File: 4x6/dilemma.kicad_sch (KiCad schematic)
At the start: 308 parts, among them J1 USB_C_Receptacle_USB2.0, J102 NA_serial, J105 NA_Conn_01x04_Female, J113 Cirque, J3 NA_GC9A01, J4 Conn_01x05, J5 NA_Conn_01x02, J5001 USB_C_Receptacle_USB2.0, J5002 NA_Conn_01x02, J5003 NA_serial, J5004 NA_GC9A01, J5005 NA_Conn_01x04_Female, J5007 Cirque, J5008 Conn_01x05, J5009 Conn_01x05, J5010 Conn_01x05, SW1 SW_Push, SW101 NA_SW_Push, SW102 NA_SW_Push, SW103 NA_SW_Push, SW104 NA_SW_Push, SW105 NA_SW_Push, SW106 NA_SW_Push, SW107 NA_SW_Push, SW108 NA_SW_Push, SW109 NA_SW_Push, SW112 NA_SW_Push, SW113 NA_SW_Push, SW114 NA_SW_Push, SW115 NA_SW_Push, SW116 NA_SW_Push, SW117 NA_SW_Push, SW118 NA_SW_Push, SW119 NA_SW_Push, SW3001 NA_SW_Push, SW3002 NA_RotaryEncoder_Switch, SW5001 SW_Push, SW5002 NA_SW_Push, SW5003 NA_SW_Push, SW5004 NA_SW_Push, SW5005 NA_SW_Push, SW5006 NA_SW_Push, SW5007 NA_SW_Push, SW5008 NA_SW_Push, SW5009 NA_SW_Push, SW5010 NA_SW_Push, SW5011 NA_SW_Push, SW5012 NA_SW_Push, SW5013 NA_SW_Push, SW5014 NA_SW_Push, SW5015 NA_SW_Push, SW5016 NA_SW_Push, SW5017 NA_SW_Push, SW5018 NA_SW_Push, SW5019 NA_SW_Push, SW5020 NA_RotaryEncoder_Switch, SW5021 SW_SPST, SW5022 SW_SPST, SW5023 NA_SW_Push, SW5024 NA_SW_Push, SW5025 NA_SW_Push, SW5026 NA_SW_Push, SW5027 NA_SW_Push, SW5028 NA_SW_Push, SW5029 NA_SW_Push, SW5030 NA_SW_Push, SW5031 NA_SW_Push, SW5032 NA_SW_Push, SW5033 NA_SW_Push, SW5034 NA_SW_Push, SW5035 NA_SW_Push, SW5036 NA_SW_Push, SW5037 NA_SW_Push, SW5038 NA_SW_Push, SW5039 NA_SW_Push, SW5040 NA_SW_Push, U1 RP2040, U2 W25Q128JVS, U3 XC6210B332MR-G, U4 USBLC6-2P6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

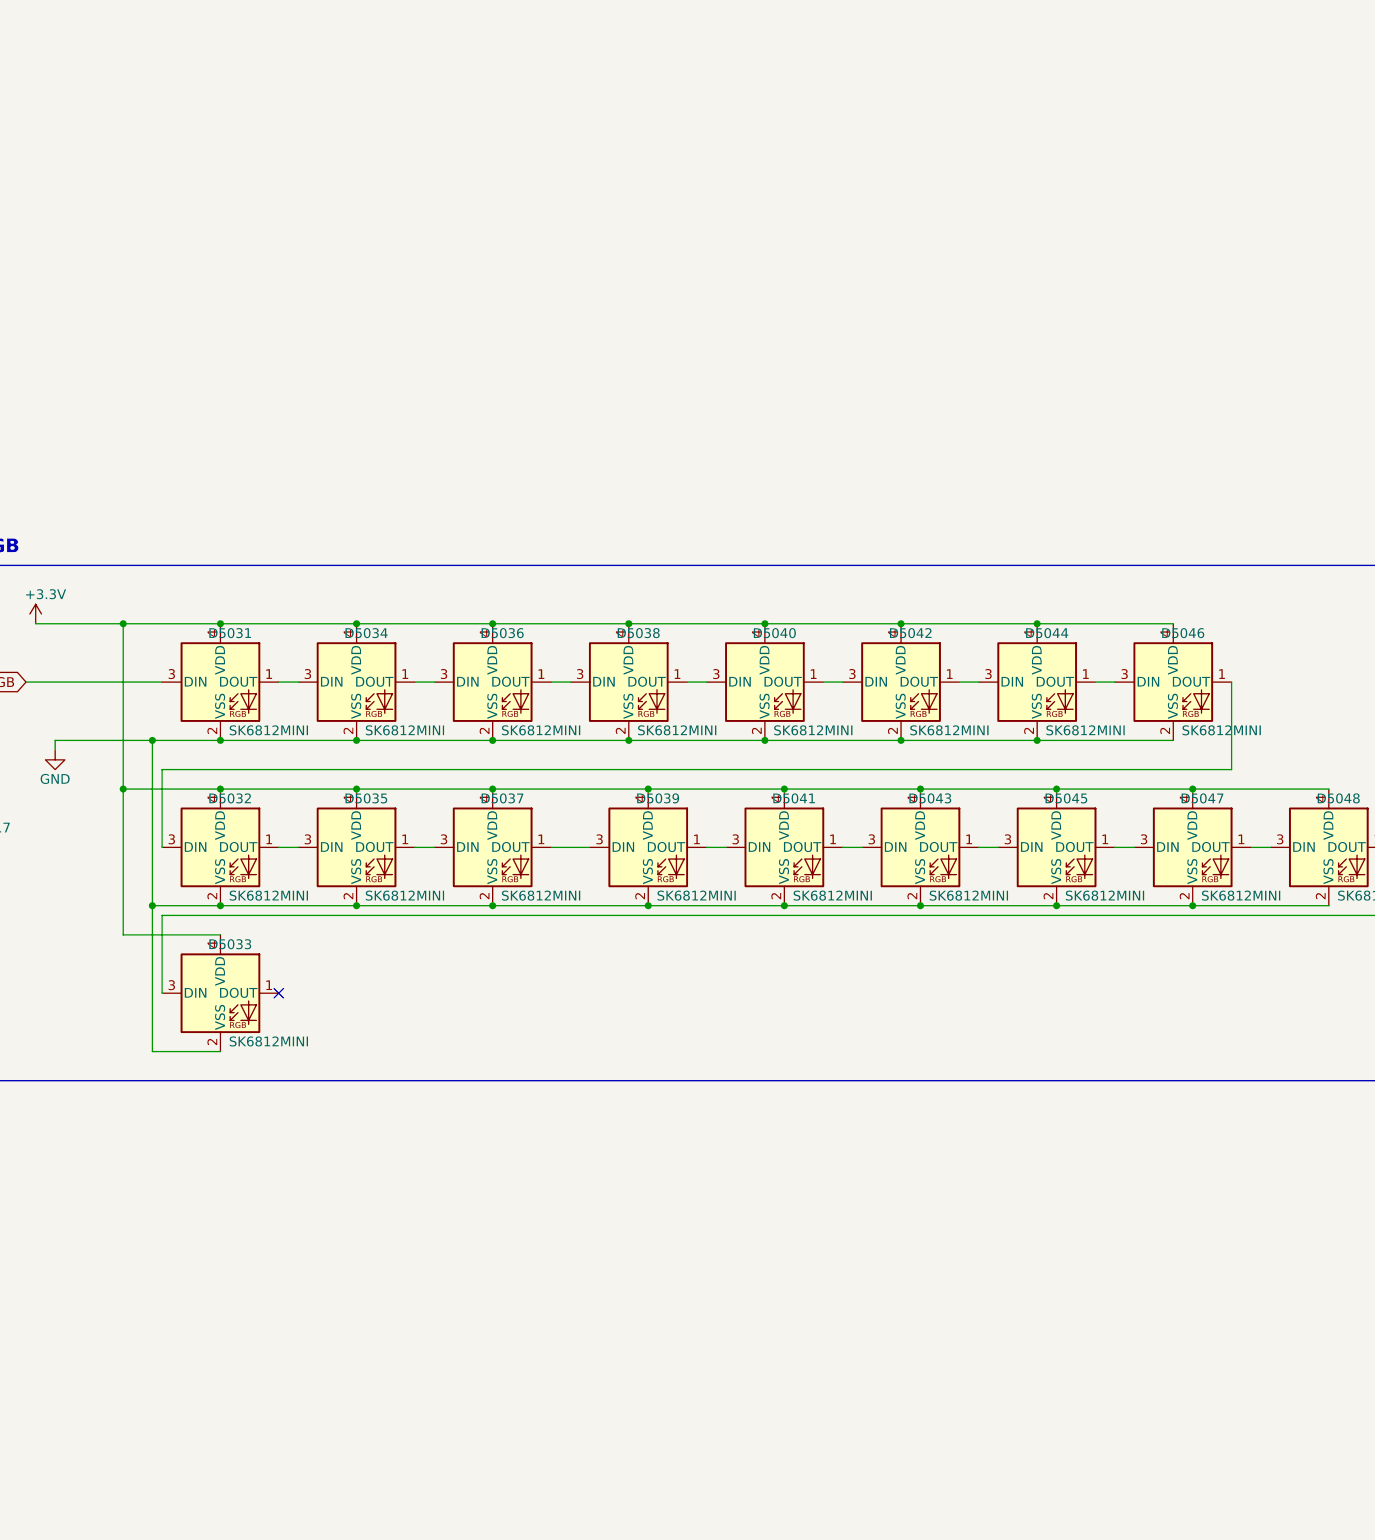
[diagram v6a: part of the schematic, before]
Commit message: place per key rgb leds right
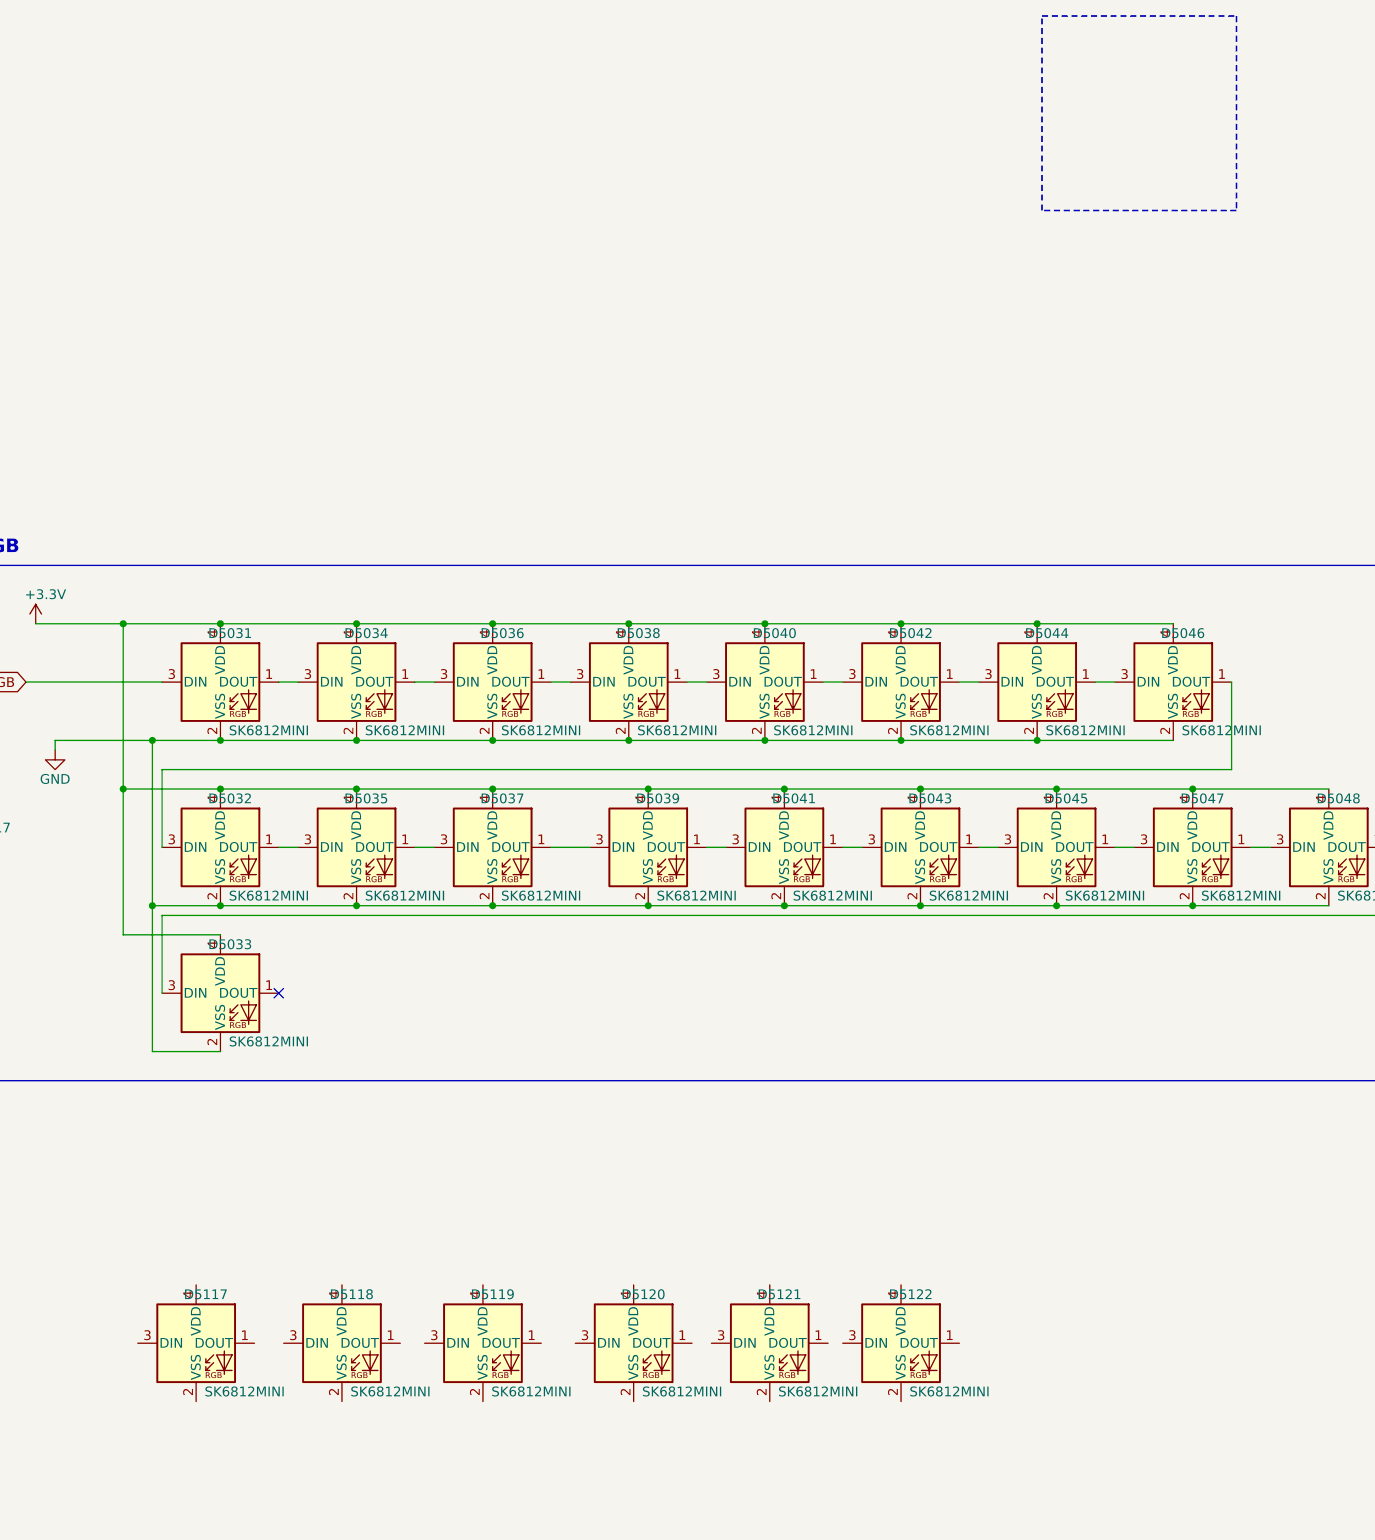
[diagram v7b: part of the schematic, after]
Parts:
- added D5117, D5118, D5119, D5120, D5121, D5122: SK6812MINI, local-libraries:SK6812_mini_e_corners, symbol LED:SK6812MINI
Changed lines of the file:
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@@
     (fill (type none))
   )
+  (rectangle (start 812.8 -50.8) (end 838.2 -25.4)
+    (stroke (width 0.2) (type dot))
+    (fill (type none))
+  )
   (text "USB-C connector" (at 15.24 315.595 0)
     (effects (font (size 1.778 1.778) (thickness 0.3556) bold) (justify left bottom))
@@
     )
   )
+  (symbol (lib_id "LED:SK6812MINI") (at 739.775 122.555 0) (unit 1)
+    (in_bom yes) (on_board yes) (dnp no)
+    (property "Reference" "D5119" (at 741.045 116.205 0)
+      (effects (font (size 1.27 1.27)))
+    )
+    (property "Value" "SK6812MINI" (at 746.125 128.905 0)
+      (effects (font (size 1.27 1.27)))
+    )
+    (property "Footprint" "local-libraries:SK6812_mini_e_corners" (at 741.045 130.175 0)
+      (effects (font (size 1.27 1.27)) (justify left top) hide)
+    )
+    (property "Datasheet" "https://cdn-shop.adafruit.com/product-files/2686/SK6812MINI_REV.01-1-2.pdf" (at 742.315 132.08 0)
+      (effects (font (size 1.27 1.27)) (justify left top) hide)
+    )
+    (pin "1")
+    (pin "2")
+    (pin "3")
+    (pin "4")
+    (instances
+      (project "dilemma"
+        (path "/7353e96a-343a-4876-b497-b1d205a14d97"
+          (reference "D5119") (unit 1)
+        )
+      )
+    )
+  )
   (symbol (lib_id "power_L:+3V3_L") (at 37.465 457.835 0) (unit 1)
     (in_bom yes) (on_board yes) (dnp no) (fields_autoplaced)
@@
     )
   )
+  (symbol (lib_id "LED:SK6812MINI") (at 702.31 122.555 0) (unit 1)
+    (in_bom yes) (on_board yes) (dnp no)
+    (property "Reference" "D5117" (at 703.58 116.205 0)
+      (effects (font (size 1.27 1.27)))
+    )
+    (property "Value" "SK6812MINI" (at 708.66 128.905 0)
+      (effects (font (size 1.27 1.27)))
+    )
+    (property "Footprint" "local-libraries:SK6812_mini_e_corners" (at 703.58 130.175 0)
+      (effects (font (size 1.27 1.27)) (justify left top) hide)
+    )
+    (property "Datasheet" "https://cdn-shop.adafruit.com/product-files/2686/SK6812MINI_REV.01-1-2.pdf" (at 704.85 132.08 0)
+      (effects (font (size 1.27 1.27)) (justify left top) hide)
+    )
+    (pin "1")
+    (pin "2")
+    (pin "3")
+    (pin "4")
+    (instances
+      (project "dilemma"
+        (path "/7353e96a-343a-4876-b497-b1d205a14d97"
+          (reference "D5117") (unit 1)
+        )
+      )
+    )
+  )
   (symbol (lib_id "Device:LED") (at 22.225 467.995 90) (unit 1)
     (in_bom yes) (on_board yes) (dnp no)
@@
     )
   )
+  (symbol (lib_id "LED:SK6812MINI") (at 721.36 122.555 0) (unit 1)
+    (in_bom yes) (on_board yes) (dnp no)
+    (property "Reference" "D5118" (at 722.63 116.205 0)
+      (effects (font (size 1.27 1.27)))
+    )
+    (property "Value" "SK6812MINI" (at 727.71 128.905 0)
+      (effects (font (size 1.27 1.27)))
+    )
+    (property "Footprint" "local-libraries:SK6812_mini_e_corners" (at 722.63 130.175 0)
+      (effects (font (size 1.27 1.27)) (justify left top) hide)
+    )
+    (property "Datasheet" "https://cdn-shop.adafruit.com/product-files/2686/SK6812MINI_REV.01-1-2.pdf" (at 723.9 132.08 0)
+      (effects (font (size 1.27 1.27)) (justify left top) hide)
+    )
+    (pin "1")
+    (pin "2")
+    (pin "3")
+    (pin "4")
+    (instances
+      (project "dilemma"
+        (path "/7353e96a-343a-4876-b497-b1d205a14d97"
+          (reference "D5118") (unit 1)
+        )
+      )
+    )
+  )
   (symbol (lib_id "power_L:GND_L") (at 181.61 474.345 0) (unit 1)
     (in_bom yes) (on_board yes) (dnp no) (fields_autoplaced)
@@
     )
   )
+  (symbol (lib_id "LED:SK6812MINI") (at 759.46 122.555 0) (unit 1)
+    (in_bom yes) (on_board yes) (dnp no)
+    (property "Reference" "D5120" (at 760.73 116.205 0)
+      (effects (font (size 1.27 1.27)))
+    )
+    (property "Value" "SK6812MINI" (at 765.81 128.905 0)
+      (effects (font (size 1.27 1.27)))
+    )
+    (property "Footprint" "local-libraries:SK6812_mini_e_corners" (at 760.73 130.175 0)
+      (effects (font (size 1.27 1.27)) (justify left top) hide)
+    )
+    (property "Datasheet" "https://cdn-shop.adafruit.com/product-files/2686/SK6812MINI_REV.01-1-2.pdf" (at 762 132.08 0)
+      (effects (font (size 1.27 1.27)) (justify left top) hide)
+    )
+    (pin "1")
+    (pin "2")
+    (pin "3")
+    (pin "4")
+    (instances
+      (project "dilemma"
+        (path "/7353e96a-343a-4876-b497-b1d205a14d97"
+          (reference "D5120") (unit 1)
+        )
+      )
+    )
+  )
   (symbol (lib_id "power_L:GND_L") (at 693.42 348.615 0) (unit 1)
     (in_bom yes) (on_board yes) (dnp no) (fields_autoplaced)
@@
     )
   )
+  (symbol (lib_id "LED:SK6812MINI") (at 777.24 122.555 0) (unit 1)
+    (in_bom yes) (on_board yes) (dnp no)
+    (property "Reference" "D5121" (at 778.51 116.205 0)
+      (effects (font (size 1.27 1.27)))
+    )
+    (property "Value" "SK6812MINI" (at 783.59 128.905 0)
+      (effects (font (size 1.27 1.27)))
+    )
+    (property "Footprint" "local-libraries:SK6812_mini_e_corners" (at 778.51 130.175 0)
+      (effects (font (size 1.27 1.27)) (justify left top) hide)
+    )
+    (property "Datasheet" "https://cdn-shop.adafruit.com/product-files/2686/SK6812MINI_REV.01-1-2.pdf" (at 779.78 132.08 0)
+      (effects (font (size 1.27 1.27)) (justify left top) hide)
+    )
+    (pin "1")
+    (pin "2")
+    (pin "3")
+    (pin "4")
+    (instances
+      (project "dilemma"
+        (path "/7353e96a-343a-4876-b497-b1d205a14d97"
+          (reference "D5121") (unit 1)
+        )
+      )
+    )
+  )
   (symbol (lib_id "LED:SK6812MINI") (at 794.385 36.195 0) (unit 1)
     (in_bom yes) (on_board yes) (dnp no)
@@
         )
       )
+    )
+  )
+  (symbol (lib_id "LED:SK6812MINI") (at 794.385 122.555 0) (unit 1)
+    (in_bom yes) (on_board yes) (dnp no)
+    (property "Reference" "D5122" (at 795.655 116.205 0)
+      (effects (font (size 1.27 1.27)))
+    )
+    (property "Value" "SK6812MINI" (at 800.735 128.905 0)
+      (effects (font (size 1.27 1.27)))
+    )
+    (property "Footprint" "local-libraries:SK6812_mini_e_corners" (at 795.655 130.175 0)
+      (effects (font (size 1.27 1.27)) (justify left top) hide)
+    )
+    (property "Datasheet" "https://cdn-shop.adafruit.com/product-files/2686/SK6812MINI_REV.01-1-2.pdf" (at 796.925 132.08 0)
+      (effects (font (size 1.27 1.27)) (justify left top) hide)
+    )
+    (pin "1")
+    (pin "2")
+    (pin "3")
+    (pin "4")
+    (instances
+      (project "dilemma"
+        (path "/7353e96a-343a-4876-b497-b1d205a14d97"
+          (reference "D5122") (unit 1)
+        )
+      )

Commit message: plate per key rgb right side
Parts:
- added D5123, D5124, D5125, D5127: SK6812MINI, local-libraries:SK6812_mini_e_corners, symbol LED:SK6812MINI
- added D5126: D_matrix, local-libraries:D_0402, symbol Device:D
- added SW5041: NA_SW_Push, local-libraries:SW_MX_choc, symbol Switch:SW_Push
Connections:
- net +3V3: now also D5117.4 (VDD), D5118.4 (VDD), D5119.4 (VDD), D5120.4 (VDD), D5121.4 (VDD), D5122.4 (VDD), D5123.4 (VDD), D5124.4 (VDD), D5125.4 (VDD)
- net GND: now also D5117.2 (VSS), D5118.2 (VSS), D5119.2 (VSS), D5120.2 (VSS), D5121.2 (VSS), D5122.2 (VSS), D5123.2 (VSS), D5124.2 (VSS), D5125.2 (VSS), D5127.2 (VSS)
- net M_COL4: now also D5126.1 (K)
- net M_ROW1: now also SW5041.1
- net RGB: now also D5117.3 (DIN); no longer D5031.3 (DIN)
- net at D5031.1 (DOUT): now also D5035.3 (DIN); no longer D5034.3 (DIN)
- net at D5033.1 (DOUT): now also D5127.3 (DIN)
- net at D5036.1 (DOUT): now also D5034.3 (DIN); no longer D5038.3 (DIN)
- net at D5034.1 (DOUT): now also D5031.3 (DIN); no longer D5036.3 (DIN)
- net at D5040.1 (DOUT): now also D5038.3 (DIN); no longer D5042.3 (DIN)
- net at D5038.1 (DOUT): now also D5036.3 (DIN); no longer D5040.3 (DIN)
- net at D5119.1 (DOUT): now also D5118.3 (DIN)
- net at D5119.3 (DIN): now also D5120.1 (DOUT)
- net at D5032.1 (DOUT): now also D5046.3 (DIN); no longer D5035.3 (DIN)
- net at D5032.3 (DIN): now also D5035.1 (DOUT); no longer D5046.1 (DOUT)
- net at D5043.1 (DOUT): now also D5041.3 (DIN); no longer D5045.3 (DIN)
- net at D5043.3 (DIN): now also D5045.1 (DOUT); no longer D5041.1 (DOUT)
- net at D5037.3 (DIN): now also D5039.1 (DOUT); no longer D5035.1 (DOUT)
- net at D5117.1 (DOUT): now also D5122.3 (DIN)
- net at D5118.1 (DOUT): now also D5123.3 (DIN)
- net at D5039.3 (DIN): now also D5041.1 (DOUT); no longer D5037.1 (DOUT)
- net at D5120.3 (DIN): now also D5121.1 (DOUT)
- net at D5047.3 (DIN): now also D5037.1 (DOUT); no longer D5045.1 (DOUT)
- net at D5044.1 (DOUT): now also D5042.3 (DIN); no longer D5046.3 (DIN)
- net at D5121.3 (DIN): now also D5122.1 (DOUT)
- net at D5042.1 (DOUT): now also D5124.3 (DIN); no longer D5044.3 (DIN)
- new net: D5040.3 (DIN), D5123.1 (DOUT)
- new net: D5126.2 (A), SW5041.2
- new net: D5124.1 (DOUT), D5125.3 (DIN)
- new net: D5044.3 (DIN), D5046.1 (DOUT)
- new net: D5045.3 (DIN), D5125.1 (DOUT)
- no-connect marks 26 -> 27
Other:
- moved on the sheet: C5017, D5031, D5032, D5033, D5034, D5035, D5036, D5037, D5038, D5039, D5040, D5041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
